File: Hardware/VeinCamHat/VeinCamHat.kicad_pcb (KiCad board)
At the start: 2 copper layers, 65 x 56 mm, 5 parts, among them P1 Conn_02x20_Odd_Even

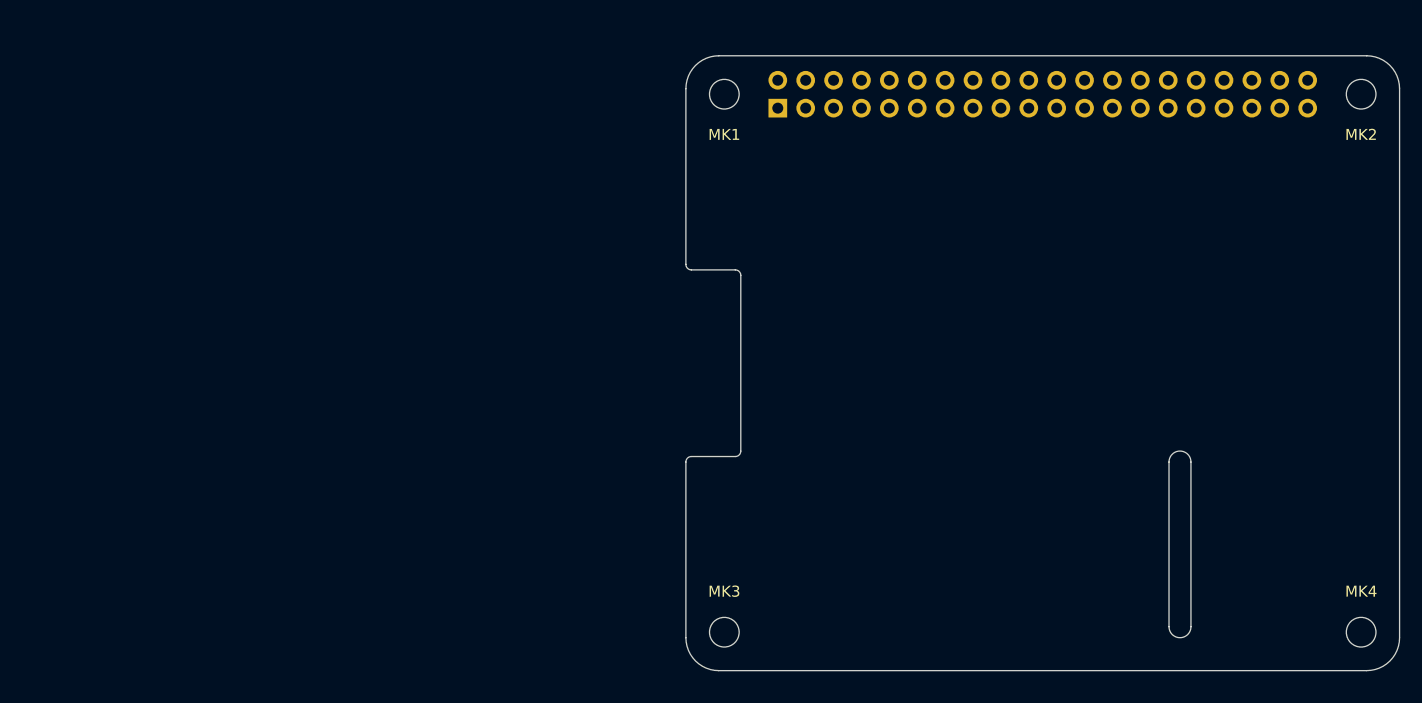
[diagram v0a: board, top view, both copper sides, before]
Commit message: Added footprints for VeinCamHat and begun layout
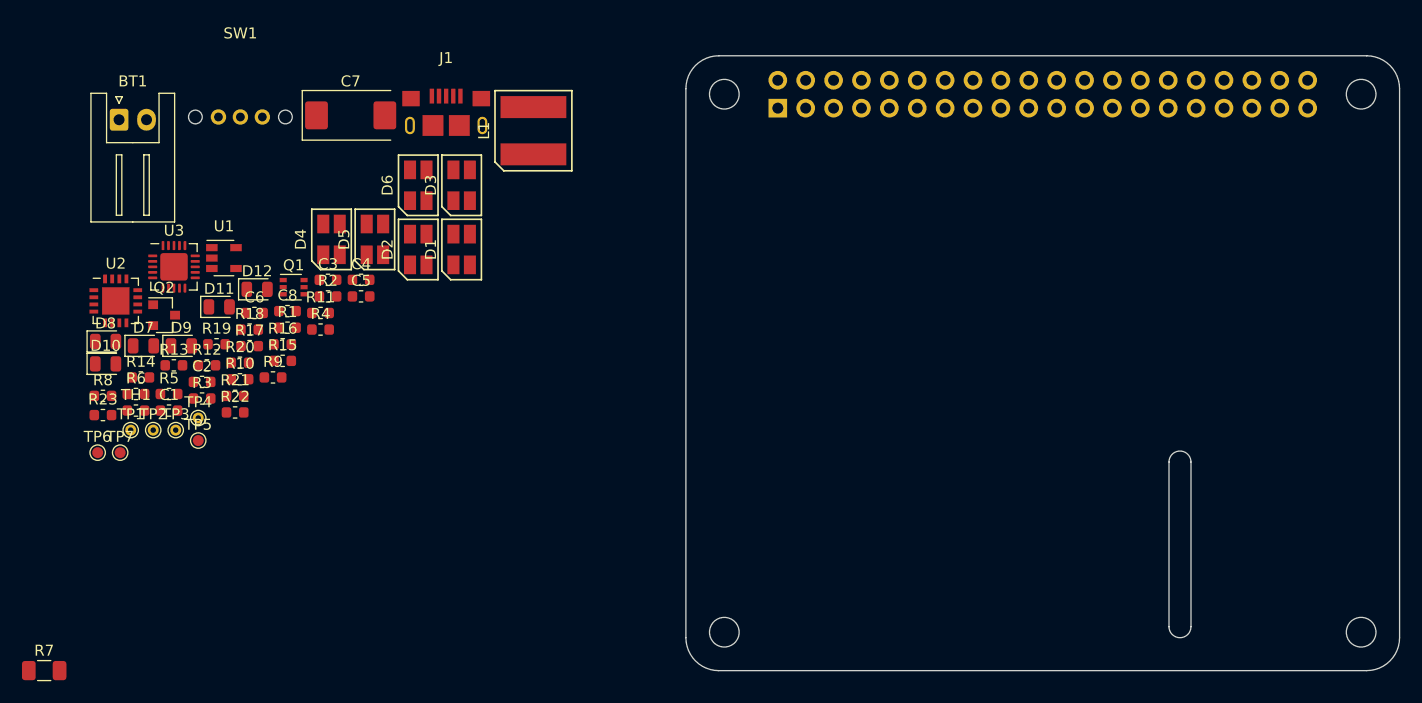
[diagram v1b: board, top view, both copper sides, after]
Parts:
- removed MK1, MK2, MK3, MK4: M2.5, MountingHole:MountingHole_2.7mm_M2.5
- removed P1: Conn_02x20_Odd_Even, Connector_PinSocket_2.54mm:PinSocket_2x20_P2.54mm_Vertical
- added BT1: 3v7 LIPO, Connector_JST:JST_XH_S02B-XH-A_1x02_P2.50mm_Horizontal, F.Cu at (148.4, 99.8)
- added C1: 10u, Capacitor_SMD:C_0603_1608Metric, F.Cu at (152.9, 126.3)
- added C2: 100n, Capacitor_SMD:C_0603_1608Metric, F.Cu at (155.9, 123.7)
- added C3: 10u, Capacitor_SMD:C_0603_1608Metric, F.Cu at (167.4, 114.4)
- added C4: 10u, Capacitor_SMD:C_0603_1608Metric, F.Cu at (170.4, 114.4)
- added C5: 100n, Capacitor_SMD:C_0603_1608Metric, F.Cu at (170.4, 115.9)
- added C6: 2u2, Capacitor_SMD:C_0603_1608Metric, F.Cu at (160.7, 117.4)
- added C7: 100u, Capacitor_Tantalum_SMD:CP_EIA-7343-31_Kemet-D, F.Cu at (169.5, 99.4)
- added C8: 10u, Capacitor_SMD:C_0603_1608Metric, F.Cu at (163.7, 117.3)
- added D1: SFH7252, VeinCam_Footprints:SFH7252, F.Cu at (179.6, 111.6)
- added D10: RED LED, LED_SMD:LED_0805_2012Metric, F.Cu at (147.1, 122.1)
- added D11: GREEN LED, LED_SMD:LED_0805_2012Metric, F.Cu at (157.5, 116.9)
- added D12: RED LED, LED_SMD:LED_0805_2012Metric, F.Cu at (160.9, 115.3)
- added D2: SFH7252, VeinCam_Footprints:SFH7252, F.Cu at (175.6, 111.6)
- added D3: SFH7252, VeinCam_Footprints:SFH7252, F.Cu at (179.6, 105.8)
- added D4: SFH7252, VeinCam_Footprints:SFH7252, F.Cu at (167.7, 110.7)
- added D5: SFH7252, VeinCam_Footprints:SFH7252, F.Cu at (171.7, 110.7)
- added D6: SFH7252, VeinCam_Footprints:SFH7252, F.Cu at (175.6, 105.8)
- added D7: GREEN LED, LED_SMD:LED_0805_2012Metric, F.Cu at (150.6, 120.4)
- added D8: RED LED, LED_SMD:LED_0805_2012Metric, F.Cu at (147.1, 120.0)
- added D9: GREEN LED, LED_SMD:LED_0805_2012Metric, F.Cu at (154.0, 120.4)
- added H1: MountingHole, MountingHole:MountingHole_2.7mm_M2.5, F.Cu at (203.5, 97.5)
- added H2: MountingHole, MountingHole:MountingHole_2.7mm_M2.5, F.Cu at (203.5, 146.5)
- added H3: MountingHole, MountingHole:MountingHole_2.7mm_M2.5, F.Cu at (261.5, 146.5)
- added H4: MountingHole, MountingHole:MountingHole_2.7mm_M2.5, F.Cu at (261.5, 97.5)
- added J1: 10118193-0001LF, VeinCam_Footprints:10118193-0001LF, F.Cu at (178.2, 101.8)
- added J2: Raspberry_Pi_2_3, Connector_PinSocket_2.54mm:PinSocket_2x20_P2.54mm_Vertical, B.Cu at (208.4, 98.8)
- added L1: SRN6045-6R8Y, VeinCam_Footprints:SRN6045, F.Cu at (186.1, 100.8)
- added Q1: BSD235N, Package_TO_SOT_SMD:SOT-363_SC-70-6, F.Cu at (164.3, 115.1)
- added Q2: MMUN2133L, Package_TO_SOT_SMD:SOT-23, F.Cu at (152.5, 117.6)
- added R1: 0R0, Resistor_SMD:R_0603_1608Metric, F.Cu at (163.7, 118.8)
- added R10: 10k, Resistor_SMD:R_0603_1608Metric, F.Cu at (159.4, 123.5)
- added R11: 1k, Resistor_SMD:R_0603_1608Metric, F.Cu at (166.7, 117.4)
- added R12: 1k, Resistor_SMD:R_0603_1608Metric, F.Cu at (156.4, 122.2)
- added R13: 1k, Resistor_SMD:R_0603_1608Metric, F.Cu at (153.4, 122.2)
- added R14: 10k, Resistor_SMD:R_0603_1608Metric, F.Cu at (150.4, 123.3)
- added R15: 1k, Resistor_SMD:R_0603_1608Metric, F.Cu at (163.3, 121.8)
- added R16: 1k, Resistor_SMD:R_0603_1608Metric, F.Cu at (163.3, 120.3)
- added R17: 1M87, Resistor_SMD:R_0603_1608Metric, F.Cu at (160.3, 120.4)
- added R18: 340k, Resistor_SMD:R_0603_1608Metric, F.Cu at (160.3, 118.9)
- added R19: 270k, Resistor_SMD:R_0603_1608Metric, F.Cu at (157.3, 120.3)
- added R2: DNP, Resistor_SMD:R_0603_1608Metric, F.Cu at (167.4, 115.9)
- added R20: 100k, Resistor_SMD:R_0603_1608Metric, F.Cu at (159.4, 122.0)
- added R21: 1k, Resistor_SMD:R_0603_1608Metric, F.Cu at (158.9, 125.0)
- added R22: 100k, Resistor_SMD:R_0603_1608Metric, F.Cu at (158.9, 126.5)
- added R23: 1k, Resistor_SMD:R_0603_1608Metric, F.Cu at (146.9, 126.7)
- added R3: 3R3, Resistor_SMD:R_0603_1608Metric, F.Cu at (155.9, 125.2)
- added R4: 3R3, Resistor_SMD:R_0603_1608Metric, F.Cu at (166.7, 118.9)
- added R5: 3R3, Resistor_SMD:R_0603_1608Metric, F.Cu at (152.9, 124.8)
- added R6: 3R3, Resistor_SMD:R_0603_1608Metric, F.Cu at (149.9, 124.8)
- added R7: DNP, Resistor_SMD:R_1206_3216Metric, F.Cu at (141.6, 150.0)
- added R8: 10k, Resistor_SMD:R_0603_1608Metric, F.Cu at (146.9, 125.0)
- added R9: 10k, Resistor_SMD:R_0603_1608Metric, F.Cu at (162.4, 123.3)
- added SW1: SS-12D07-VG 4, VeinCam_Footprints:SS-12D07-VG4, F.Cu at (159.4, 99.6)
- added TH1: 10k NTC, Resistor_SMD:R_0603_1608Metric, F.Cu at (149.9, 126.3)
- added TP1: TestPoint, TestPoint:TestPoint_THTPad_D1.0mm_Drill0.5mm, F.Cu at (149.4, 128.1)
- added TP2: TestPoint, TestPoint:TestPoint_THTPad_D1.0mm_Drill0.5mm, F.Cu at (151.5, 128.1)
- added TP3: TestPoint, TestPoint:TestPoint_THTPad_D1.0mm_Drill0.5mm, F.Cu at (153.5, 128.1)
- added TP4: TestPoint, TestPoint:TestPoint_THTPad_D1.0mm_Drill0.5mm, F.Cu at (155.6, 127.0)
- added TP5: TP_BATT, TestPoint:TestPoint_Pad_D1.0mm, F.Cu at (155.6, 129.0)
- added TP6: TP_5V0, TestPoint:TestPoint_Pad_D1.0mm, F.Cu at (146.4, 130.1)
- added TP7: TP_VLIPO, TestPoint:TestPoint_Pad_D1.0mm, F.Cu at (148.5, 130.1)
- added U1: MCP3021, Package_TO_SOT_SMD:SOT-23-5, F.Cu at (157.9, 112.4)
- added U2: TPS61092, Package_DFN_QFN:QFN-16-1EP_4x4mm_P0.65mm_EP2.5x2.5mm, F.Cu at (148.1, 116.3)
- added U3: MCP73871, Package_DFN_QFN:QFN-20-1EP_4x4mm_P0.5mm_EP2.5x2.5mm, F.Cu at (153.4, 113.2)
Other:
- outline, holes or cut-outs redrawn
- board text removed: "DISPLAY"
- board text removed: "RASPBERRY-PI 40-PIN ADDON BOARD VIEW FROM TOP NOTE: P1 SHOULD BE FITTED ON THE REVERSE OF THE BOARD ADD EDGE CUTS FROM CAMERA AND DISPLAY PORTS AS REQUIRED"
- board text removed: "RJ45"
- board text removed: "USB"
